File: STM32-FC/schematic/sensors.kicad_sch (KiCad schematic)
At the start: 17 parts, among them U6 ICM-42688-P, U7 ICM-45686, U8 ICP-20100, U9 LIS2MDLRT

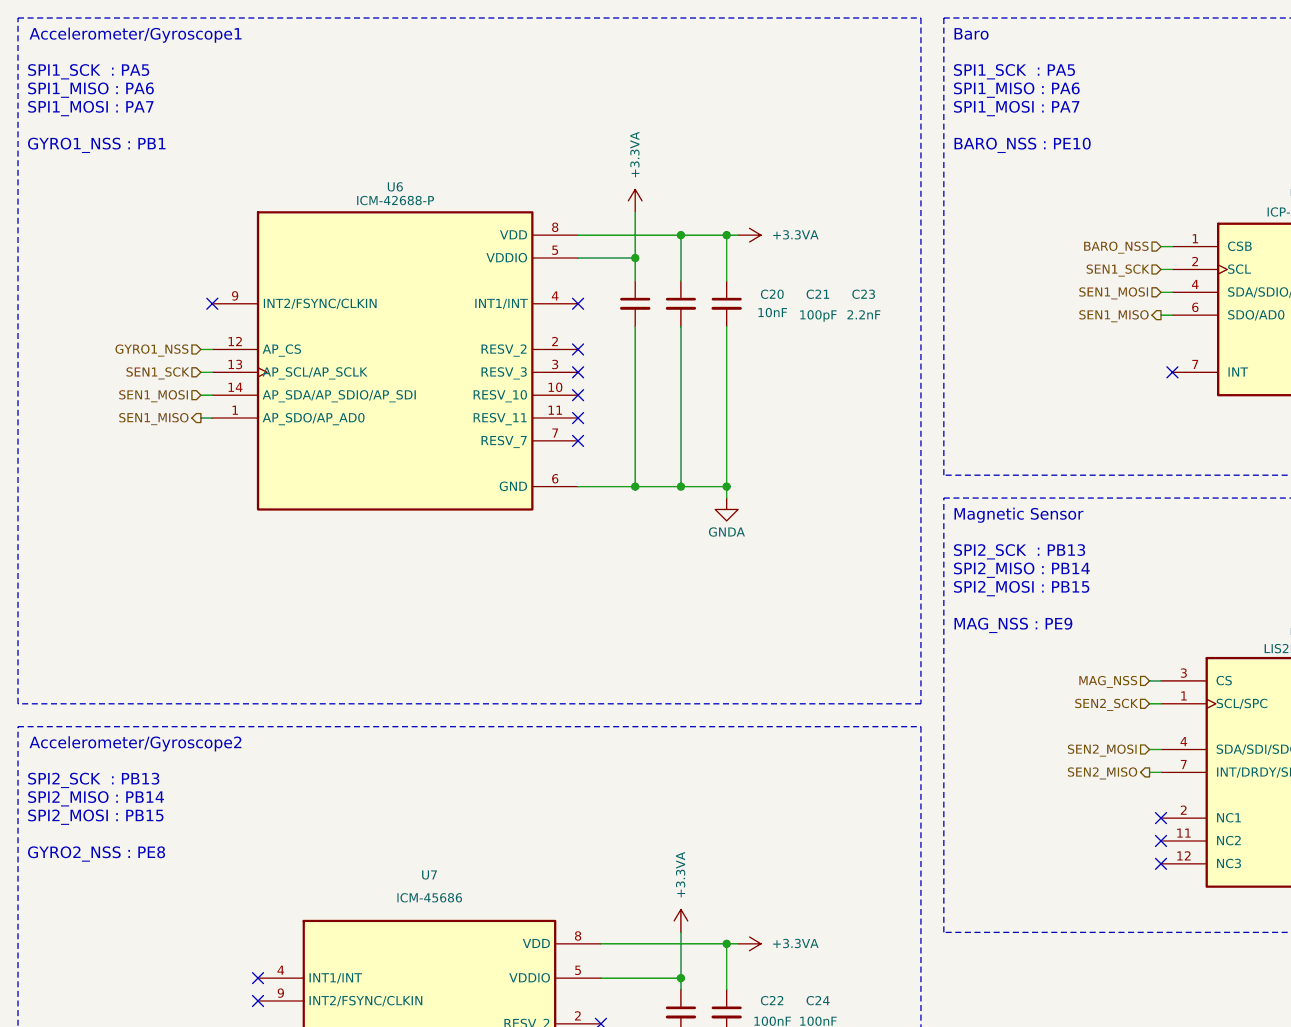
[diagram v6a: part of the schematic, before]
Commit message: fix : readme & schematic minor fix
- schematic comment fix
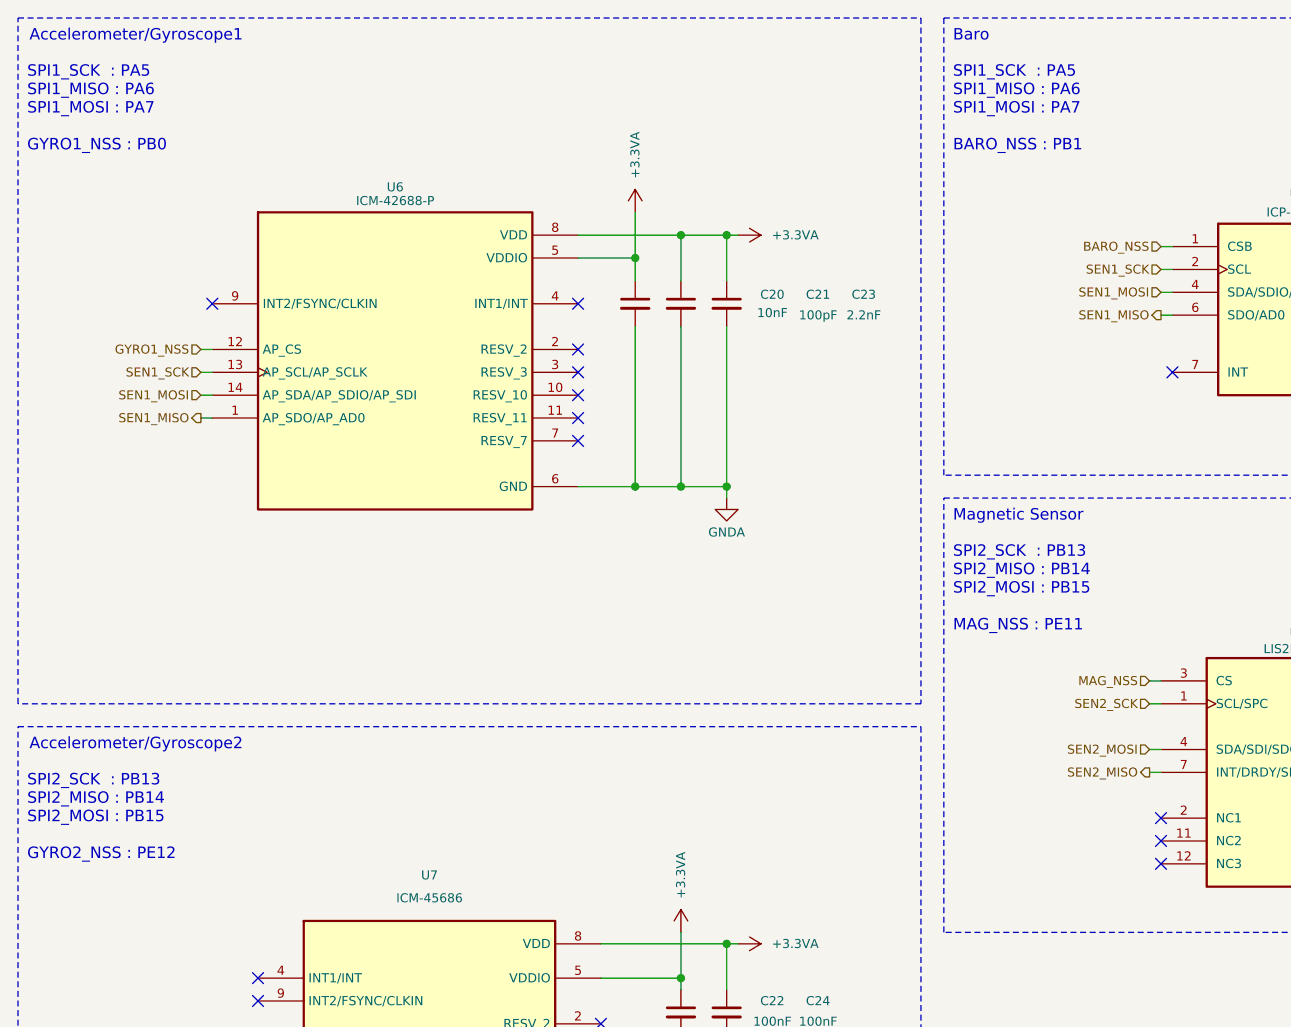
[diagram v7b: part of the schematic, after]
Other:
- note added: "SPI1_SCK : PA5 SPI1_MISO : PA6 SPI1_MOSI : PA7 BARO_NSS : PB1"
- note added: "SPI1_SCK : PA5 SPI1_MISO : PA6 SPI1_MOSI : PA7 GYRO1_NSS : PB0"
- note added: "SPI2_SCK : PB13 SPI2_MISO : PB14 SPI2_MOSI : PB15 GYRO2_NSS : PE12"
- note added: "SPI2_SCK : PB13 SPI2_MISO : PB14 SPI2_MOSI : PB15 MAG_NSS : PE11"
- note removed: "SPI1_SCK : PA5 SPI1_MISO : PA6 SPI1_MOSI : PA7 BARO_NSS : PE10"
- note removed: "SPI1_SCK : PA5 SPI1_MISO : PA6 SPI1_MOSI : PA7 GYRO1_NSS : PB1"
- note removed: "SPI2_SCK : PB13 SPI2_MISO : PB14 SPI2_MOSI : PB15 GYRO2_NSS : PE8"
- note removed: "SPI2_SCK : PB13 SPI2_MISO : PB14 SPI2_MOSI : PB15 MAG_NSS : PE9"
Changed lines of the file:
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@@
 	(title_block
 		(title "NARAEON - Flight Controller")
-		(date "2025-10-10")
+		(date "2025-10-11")
 		(rev "v1.1.0")
 		(company "NARAE")
 		(comment 1 "INHA Univ. Areo-modelling Club")
-		(comment 2 "* Work in progress")
+		(comment 2 "github.com/NARAE-INHA-UNIV")
 	)
 	(rectangle
@@
 		)
 	)
-	(text "SPI2_SCK  : PB13\nSPI2_MISO : PB14\nSPI2_MOSI : PB15\n\nGYRO2_NSS : PE8"
+	(text "SPI2_SCK  : PB13\nSPI2_MISO : PB14\nSPI2_MOSI : PB15\n\nGYRO2_NSS : PE12"
 		(exclude_from_sim no)
 		(at 23.876 96.774 0)
@@
 		)
 	)
-	(text "SPI1_SCK  : PA5\nSPI1_MISO : PA6\nSPI1_MOSI : PA7\n\nGYRO1_NSS : PB1"
+	(text "SPI1_SCK  : PA5\nSPI1_MISO : PA6\nSPI1_MOSI : PA7\n\nGYRO1_NSS : PB0"
 		(exclude_from_sim no)
 		(at 23.876 18.034 0)
@@
 		)
 	)
-	(text "SPI1_SCK  : PA5\nSPI1_MISO : PA6\nSPI1_MOSI : PA7\n\nBARO_NSS : PE10"
+	(text "SPI1_SCK  : PA5\nSPI1_MISO : PA6\nSPI1_MOSI : PA7\n\nBARO_NSS : PB1"
 		(exclude_from_sim no)
 		(at 126.746 18.034 0)
@@
 		)
 	)
-	(text "SPI2_SCK  : PB13\nSPI2_MISO : PB14\nSPI2_MOSI : PB15\n\nMAG_NSS : PE9"
+	(text "SPI2_SCK  : PB13\nSPI2_MISO : PB14\nSPI2_MOSI : PB15\n\nMAG_NSS : PE11"
 		(exclude_from_sim no)
 		(at 126.746 71.374 0)
